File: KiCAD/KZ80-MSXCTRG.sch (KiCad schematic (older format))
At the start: 17 parts, among them J1 MSX SLOT-A, J2 SBC8080 BUS, J3 SLT-JP, J4 Z80 CTRL, J5 PPI PORT-A, U1 74HC139, U2 74HC153, U3 74HC32, U4 74HC00

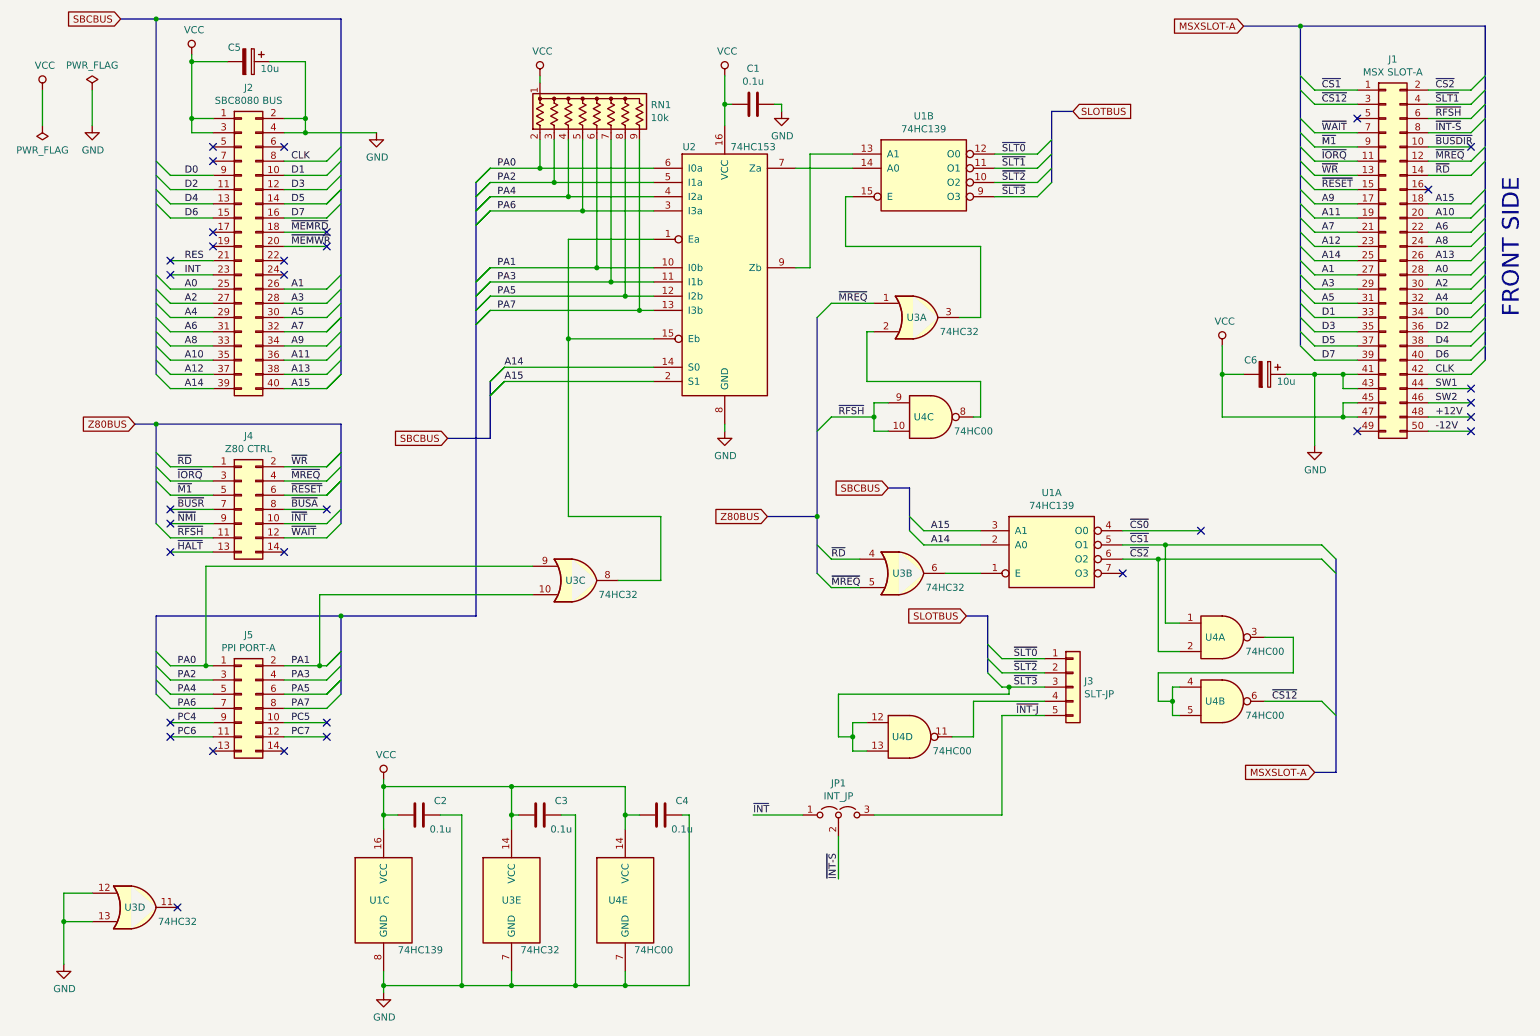
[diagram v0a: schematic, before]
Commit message: 74HC153コントロール用RS-FF追加
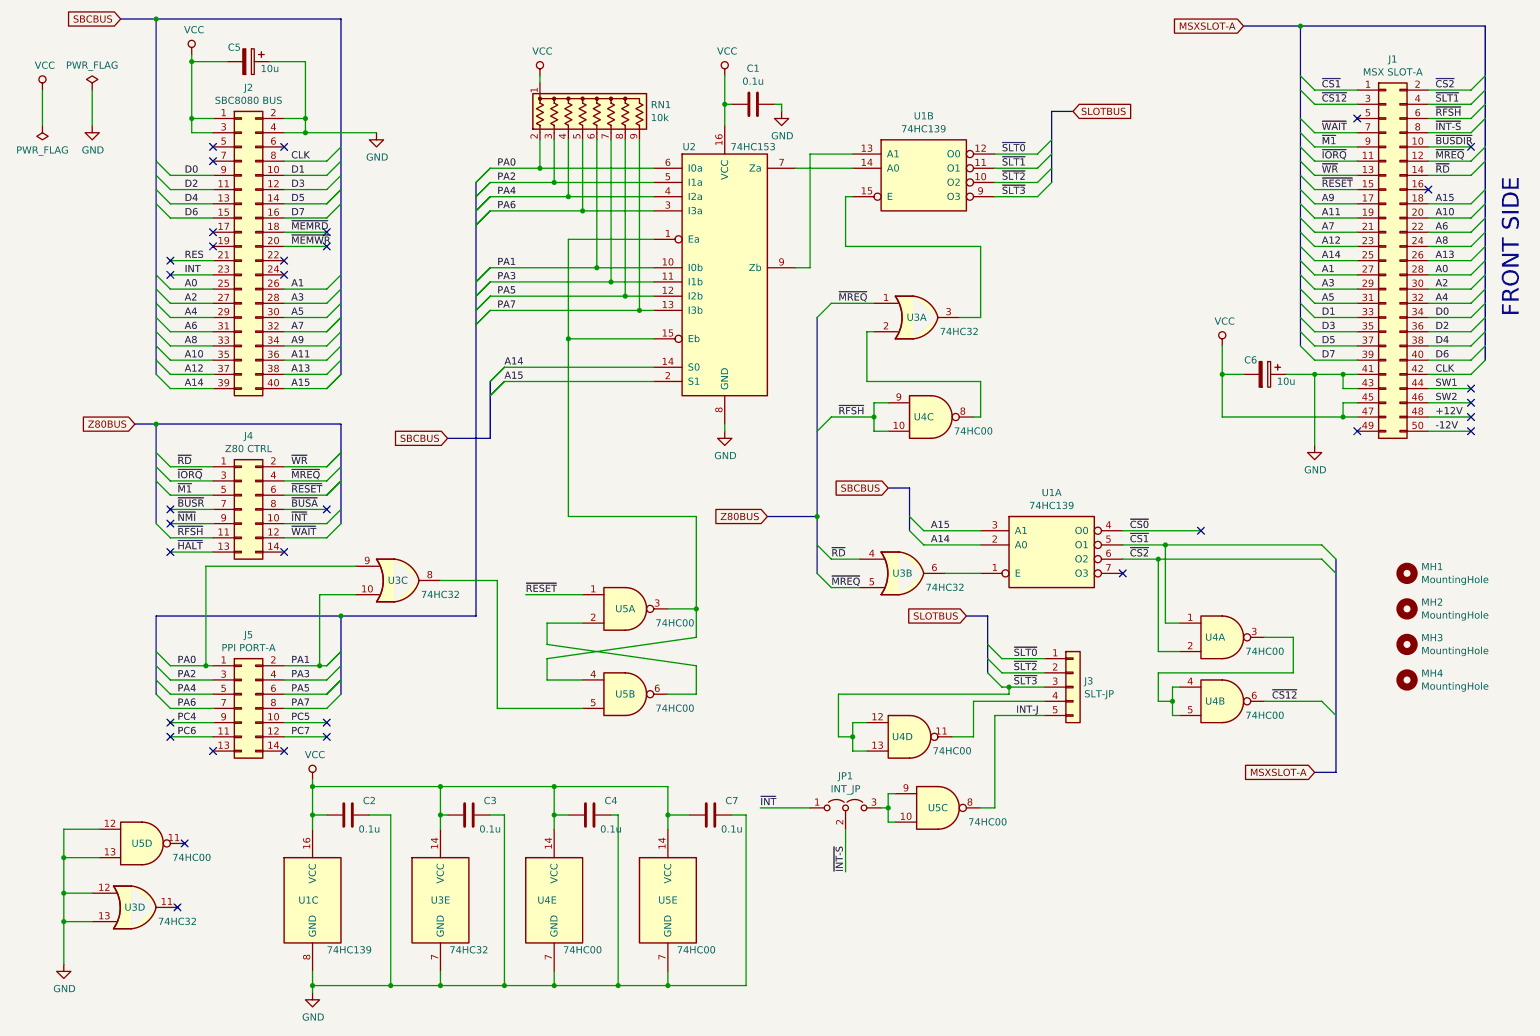
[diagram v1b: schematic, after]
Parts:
- added C7: 0.1u, Capacitor_THT:C_Disc_D3.0mm_W1.6mm_P2.50mm, symbol Device:C
- added MH1, MH2, MH3, MH4: MountingHole, MountingHole:MountingHole_3.2mm_M3, symbol Mechanical:MountingHole
- added U5: 74HC00, Package_DIP:DIP-14_W7.62mm_Socket, symbol 74xx:74HC00
- C1, C2, C3, C4: footprint (none) -> Capacitor_THT:C_Disc_D3.0mm_W1.6mm_P2.50mm
- C5, C6: footprint (none) -> Capacitor_THT:CP_Radial_D5.0mm_P2.50mm
- J1: footprint (none) -> Connector_PinHeader_2.54mm:PCB_Edge_Conn_2x25_P2.54mm_Vertical
- J2: footprint (none) -> Connector_PinHeader_2.54mm:PinHeader_2x20_P2.54mm_Horizontal
- J3: footprint (none) -> Connector_PinHeader_2.54mm:PinHeader_1x05_P2.54mm_Horizontal
- J4, J5: footprint (none) -> Connector_PinHeader_2.54mm:PinHeader_2x07_P2.54mm_Vertical
- JP1: footprint (none) -> Connector_PinHeader_2.54mm:PinHeader_1x03_P2.54mm_Vertical
- U1, U2: footprint (none) -> Package_DIP:DIP-16_W7.62mm_Socket
- U3, U4: footprint (none) -> Package_DIP:DIP-14_W7.62mm_Socket
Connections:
- net GND: now also C7.1, U5.12, U5.13, U5.7 (GND)
- net VCC: now also C7.2, U5.14 (VCC)
- net ~RESET: now also U5.1
- net at U2.1 (Ea), U2.15 (Eb): now also U5.3, U5.4; no longer U3.8
- net ~INT-J: no longer names the net of JP1.3 (B)
- net ~INT-J: now also U5.10, U5.9; no longer J3.5 (Pin_5)
- new net: U5.2, U5.6
- new net: U3.8, U5.5
- new net INT-J: J3.5 (Pin_5), U5.8
- no-connect marks 33 -> 34
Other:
- moved on the sheet: C2, C3, C4, JP1, U1C, U3C, U3E, U4E
